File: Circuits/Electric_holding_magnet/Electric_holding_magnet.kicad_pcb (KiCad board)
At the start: 2 copper layers, 38.1 x 17.8 mm, 9 parts, among them J1 Conn_01x03, Q1 BC547, Q2 BC547, SW1 SW_DIP_x01

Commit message: udated footprints npn
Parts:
- Q1, Q2: footprint Package_TO_SOT_THT:TO-92_Inline -> Package_TO_SOT_THT:TO-92_HandSolder
- renumbered L1 to E-Mag
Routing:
- net Net-(Q1-Pad2): track 8.15 -> 9.42 mm
- net Net-(Q1-Pad1): track 19.4 -> 20.6 mm

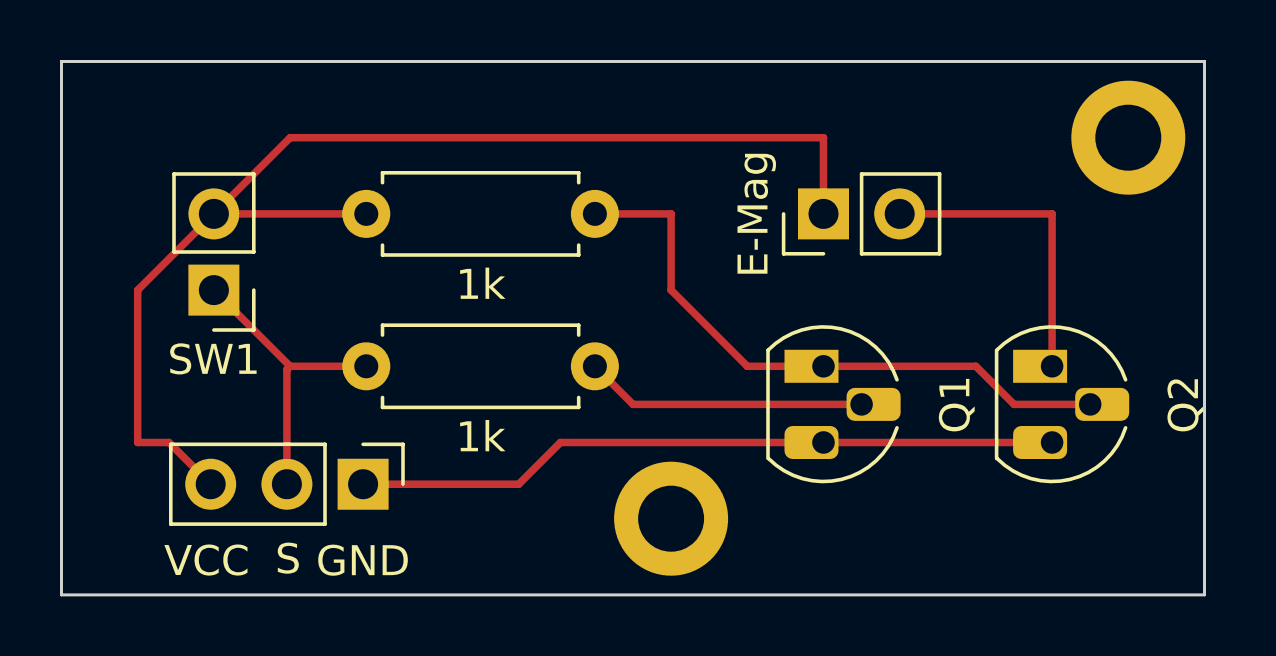
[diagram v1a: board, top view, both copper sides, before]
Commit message: update pnp footprint
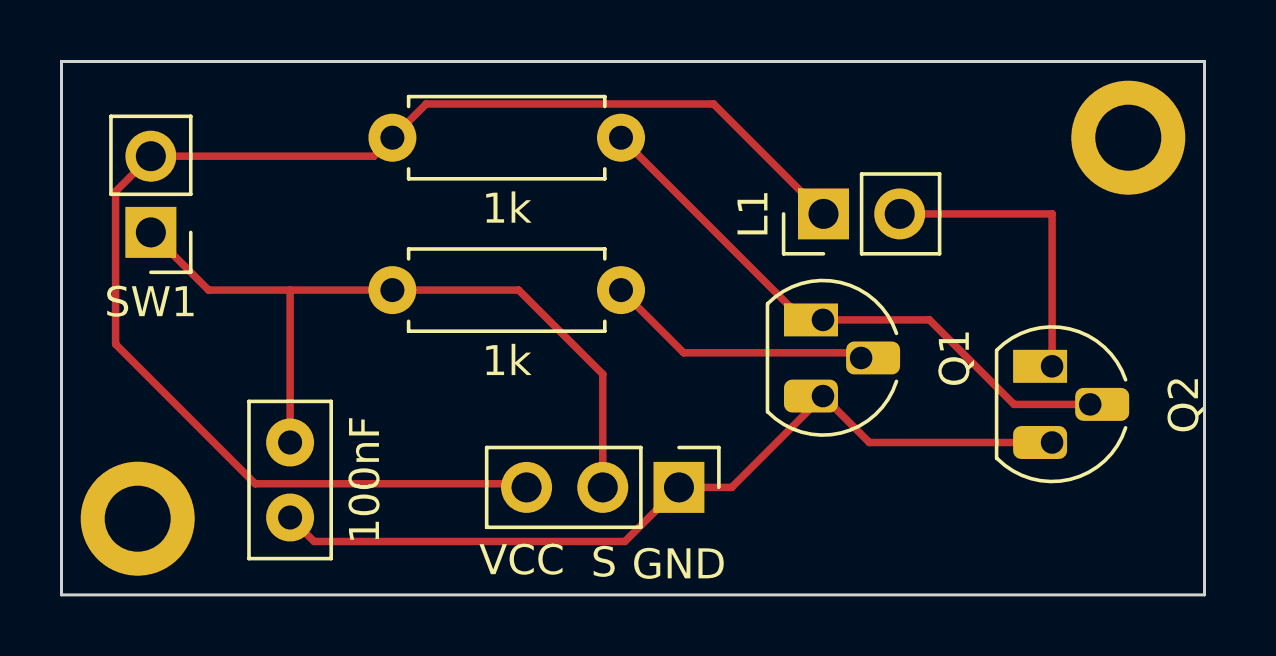
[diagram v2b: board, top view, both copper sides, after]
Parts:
- added 100nF: C, Capacitor_THT:C_Disc_D5.0mm_W2.5mm_P2.50mm, F.Cu at (116.8, 99.1)
- moved H1 17.8 mm to (111.8, 101.6)
- moved J1 10.5 mm to (129.8, 100.6)
- moved SW1 2.85 mm to (112.2, 92.1)
- moved R1 2.68 mm to (120.2, 94.0)
- moved R2 2.68 mm to (120.2, 88.9)
- moved Q1 1.55 mm to (134.6, 95.0)
- renumbered E-Mag to L1
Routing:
- net Net-(J1-Pad2): track 10.1 -> 25.9 mm
- net Net-(J1-Pad3): track 40.7 -> 47.1 mm
- net Net-(J1-Pad1): track 23.5 -> 28.4 mm
- net Net-(Q1-Pad1): track 20.6 -> 19.3 mm
- net Net-(Q1-Pad2): track 9.42 -> 8.70 mm
